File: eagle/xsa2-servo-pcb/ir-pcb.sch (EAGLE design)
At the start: 62 parts, among them IC1 ATMEGA328P-AU, IC10 SK6812_SIDE, IC11 SK6812_SIDE, IC12 SK6812_SIDE, IC13 SK6812_SIDE, IC14 SK6812_SIDE, IC15 SK6812_SIDE, IC16 SK6812_SIDE, IC17 SK6812_SIDE, IC18 SK6812_SIDE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

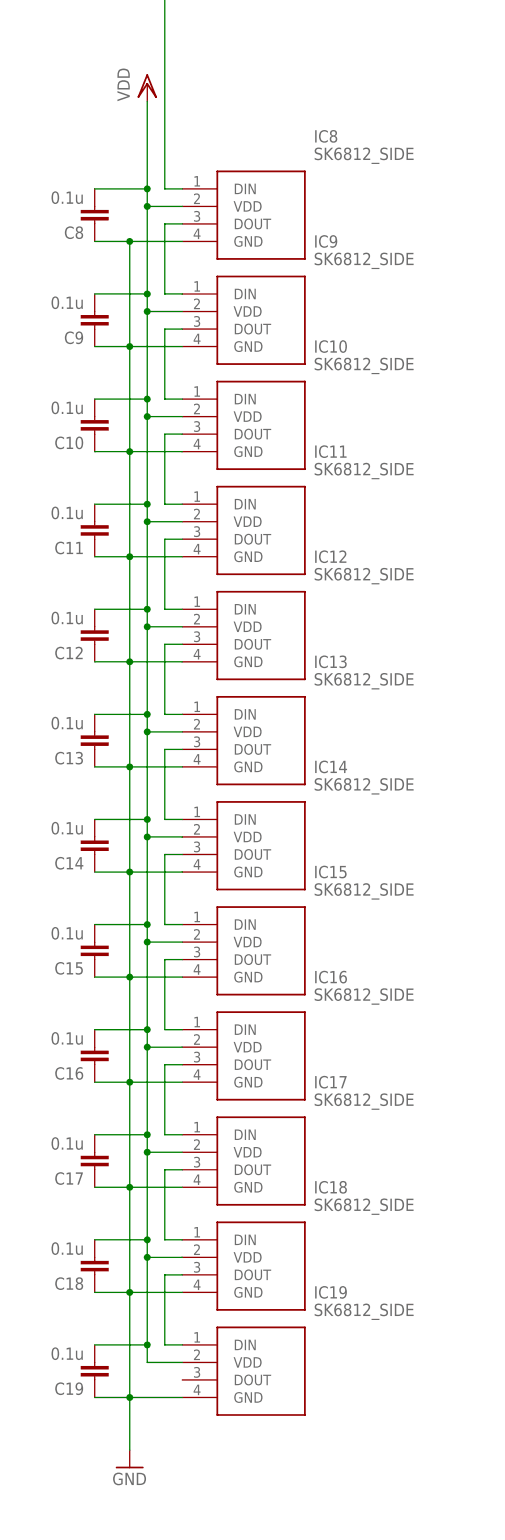
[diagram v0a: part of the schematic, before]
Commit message: [eagle] IR基板の更新
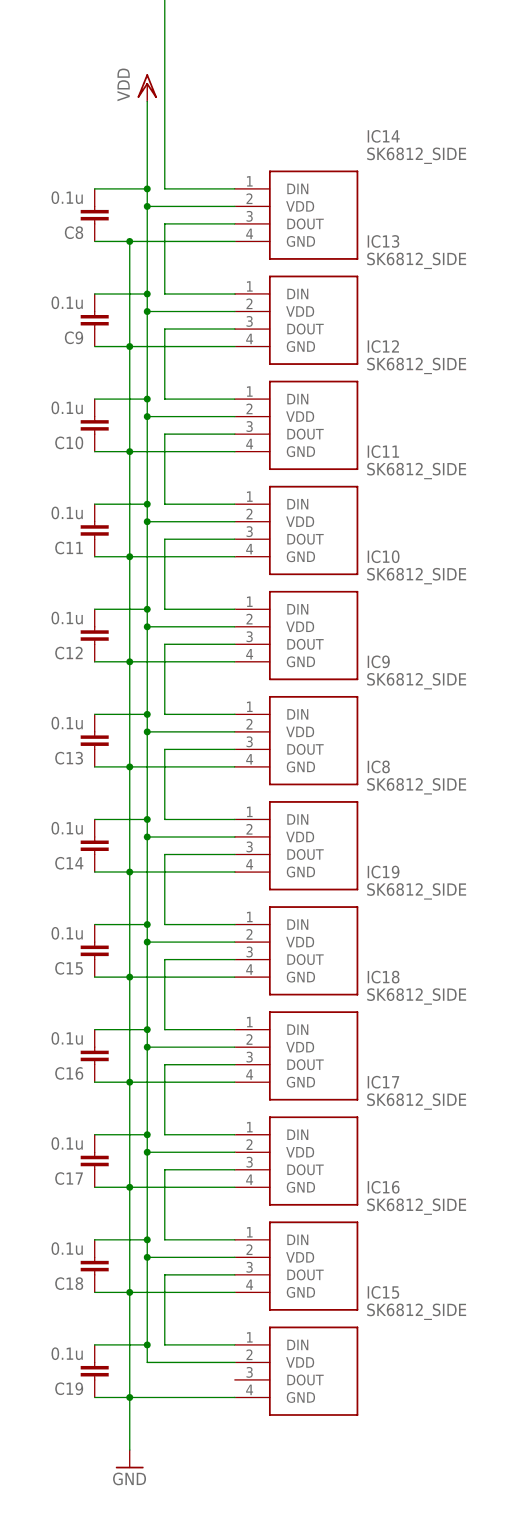
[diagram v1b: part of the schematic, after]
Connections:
- net N$12 renamed LED7
- net N$15 renamed LED8
- net N$16 renamed LED9
- net N$17 renamed LED10
- net N$27 renamed LED2
- net N$4 renamed LED1
- net N$6 renamed LED4
- net N$7 renamed LED6
- net N$8 renamed LED3
- net N$9 renamed LED5
- removed net N$35: IC13.DOUT, IC14.DIN
- new net N$11: IC8.DIN, IC9.DOUT
- net N$24: now also IC13.DIN, IC14.DOUT; no longer IC8.DOUT, IC9.DIN
- net N$31: now also IC12.DIN, IC13.DOUT; no longer IC10.DIN, IC9.DOUT
- net N$32: now also IC12.DOUT; no longer IC10.DOUT
- net N$33: now also IC10.DIN; no longer IC12.DIN
- net N$34: now also IC10.DOUT, IC9.DIN; no longer IC12.DOUT, IC13.DIN
- net N$36: now also IC19.DIN, IC8.DOUT; no longer IC14.DOUT, IC15.DIN
- net N$37: now also IC18.DIN, IC19.DOUT; no longer IC15.DOUT, IC16.DIN
- net N$38: now also IC18.DOUT; no longer IC16.DOUT
- net N$39: now also IC16.DIN; no longer IC18.DIN
- net N$40: now also IC15.DIN, IC16.DOUT; no longer IC18.DOUT, IC19.DIN
- net N$44: now also IC14.DIN; no longer IC8.DIN
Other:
- moved on the sheet: IC10, IC11, IC12, IC13, IC14, IC15, IC16, IC17, IC18, IC19, IC8, IC9
